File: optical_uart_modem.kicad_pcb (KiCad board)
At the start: 2 copper layers, 63 x 38 mm, 66 parts, among them J1 Conn_01x06_Male, Q1 KT315, Q2 Q_Photo_NPN, Q3 KT315, Q4 FDN337N, U1 74HC08, U2 LM358, U3 NE555D, U4 LM358, U5 LM339

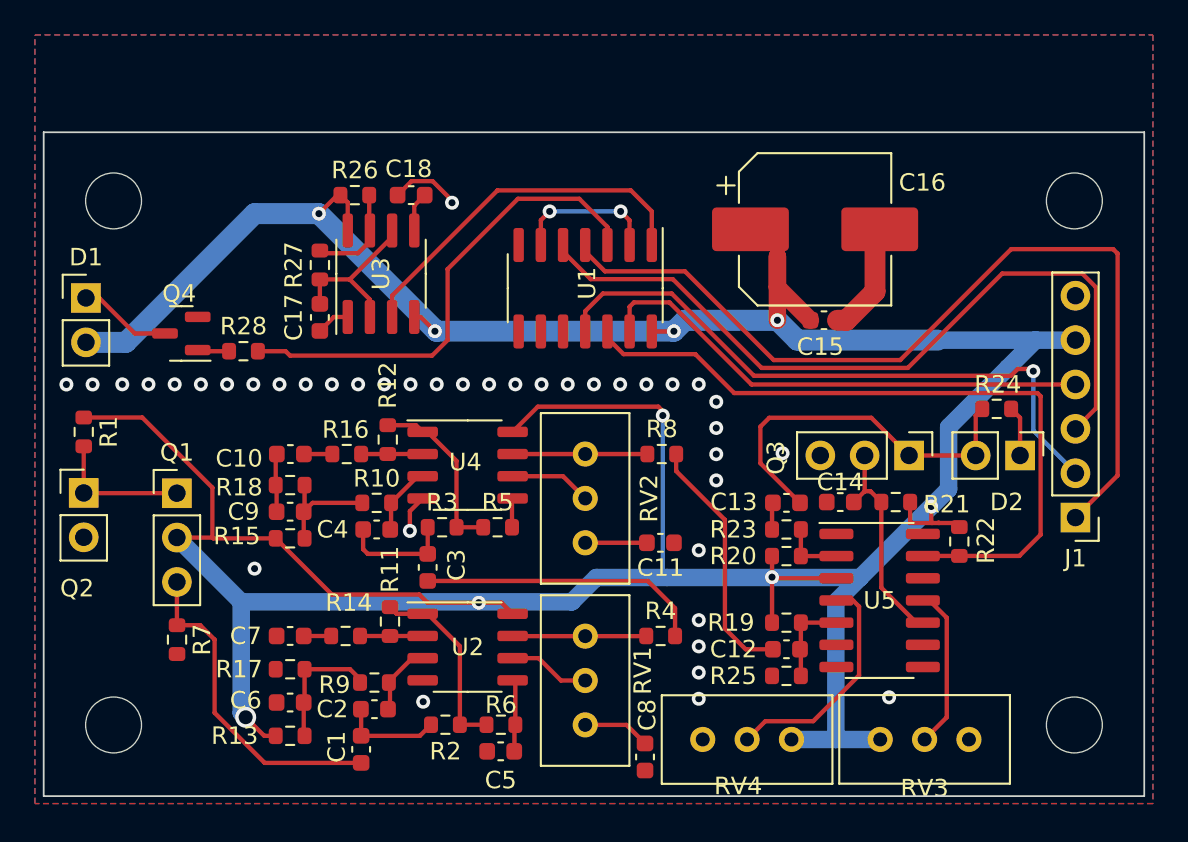
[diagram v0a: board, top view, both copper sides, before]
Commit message: test points and some silk added
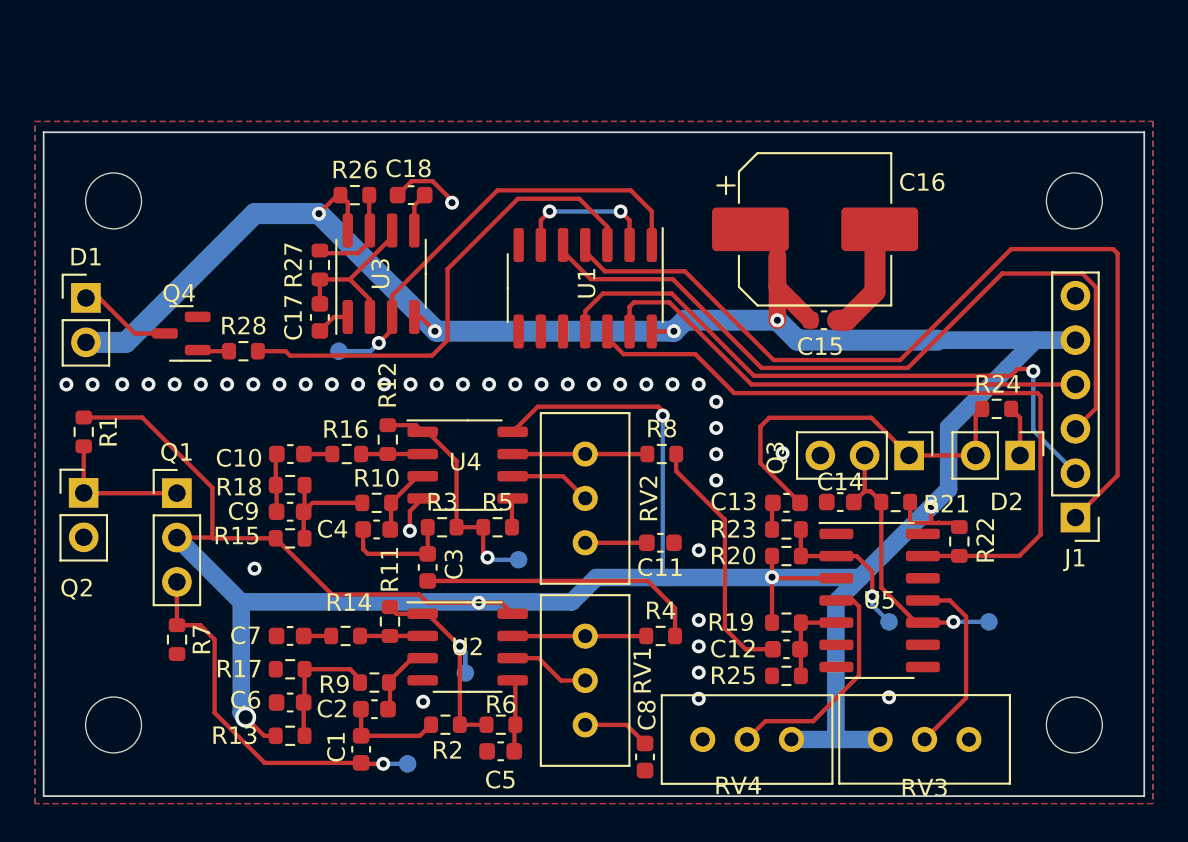
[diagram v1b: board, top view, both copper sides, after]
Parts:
- added 1st comparator output: TestPoint, TestPoint:TestPoint_Pad_D1.0mm, B.Cu at (104.4, 149.1)
- added 1st filter output: TestPoint, TestPoint:TestPoint_Pad_D1.0mm, B.Cu at (80.1, 152.0)
- added 2nd filter output: TestPoint, TestPoint:TestPoint_Pad_D1.0mm, B.Cu at (83.2, 145.5)
- added 40KHz sqare: TestPoint, TestPoint:TestPoint_Pad_D1.0mm, B.Cu at (72.9, 133.6)
- added recived signal: TestPoint, TestPoint:TestPoint_Pad_D1.0mm, B.Cu at (76.8, 157.2)
- added timer's c: TestPoint, TestPoint:TestPoint_Pad_D1.0mm, B.Cu at (110.1, 149.1)
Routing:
- net Net-(TP5-Pad1): track 3.56 -> 9.25 mm, vias 0 -> 1
- net /generator/40KHz: track 21.4 -> 25.3 mm, vias 0 -> 1
- net Net-(R12-Pad2): track 10.1 -> 13.8 mm, vias 0 -> 1
- net Net-(C14-Pad2): track 13.2 -> 16.0 mm, vias 0 -> 1
- net /recived: track 18.7 -> 21.4 mm, vias 0 -> 1
- net Net-(R11-Pad2): track 10.9 -> 12.6 mm, vias 0 -> 1
- net Net-(RV3-Pad2): track 9.28 -> 10.9 mm

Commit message: values corrected, 40KHz generator modified
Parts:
- C17: value C_Small -> 0.47n
- C18: value C_Small -> 0.01u
- R26: value R_Small -> 560K
- R27: value R_Small -> 39K
- R28: value R_Small -> 50R
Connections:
- R20 pad 1: Net-(TP5-Pad1) -> Net-(R20-Pad1)
- R23 pad 1: Net-(TP5-Pad1) -> Net-(R20-Pad1)
- R26 pad 2: Net-(R26-Pad2) -> Net-(C17-Pad1)
- R27 pad 1: Net-(R26-Pad2) -> /generator/40KHz
- U3 pad 7: Net-(R26-Pad2) -> unconnected-(U3-Pad7)
- U5 pad 2: Net-(TP5-Pad1) -> Net-(R20-Pad1)
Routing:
- net Net-(TP5-Pad1): track 9.25 -> 0.00 mm, vias 1 -> 0
- net Net-(R20-Pad1): track 0.00 -> 9.25 mm, vias 0 -> 1
- net Net-(C17-Pad1): track 9.54 -> 18.4 mm
- net Net-(R26-Pad2): track 5.86 -> 0.00 mm
- net /generator/40KHz: track 25.3 -> 30.5 mm
- net unconnected-(U3-Pad7): track 0.00 -> 0.67 mm
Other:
- board text added: "+5v"
- board text added: "GND"
- board text added: "Light -"
- board text added: "RX data"
- board text added: "RX_permition"
- board text added: "TX data"
- board text added: "TX permition"
- board text added: "light +"
- board text added: "sensor +"
- board text added: "sensor -"
